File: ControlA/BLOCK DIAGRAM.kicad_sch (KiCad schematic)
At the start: 0 parts

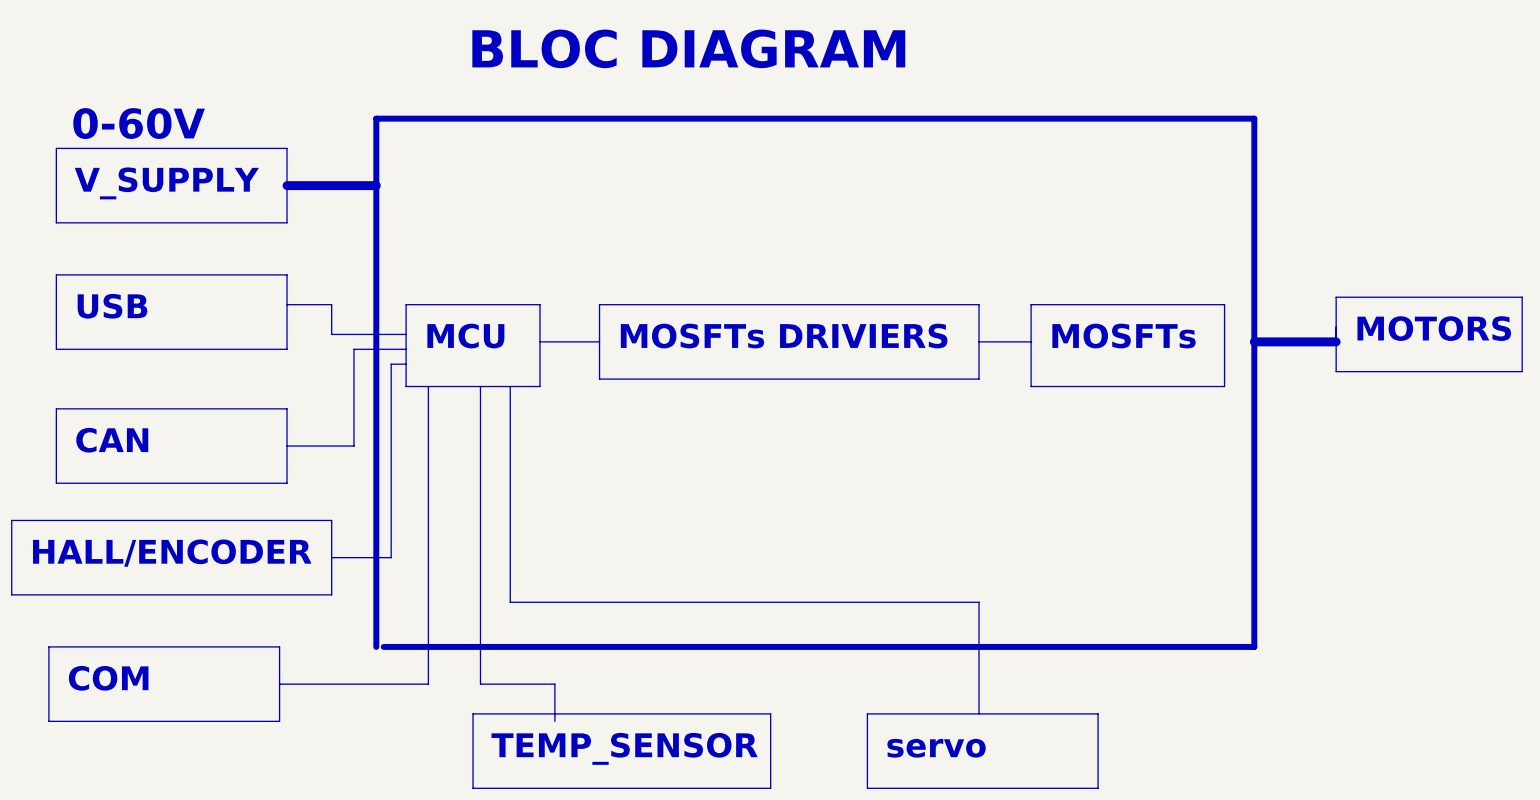
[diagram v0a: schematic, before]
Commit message: add libray symbole and add sheet
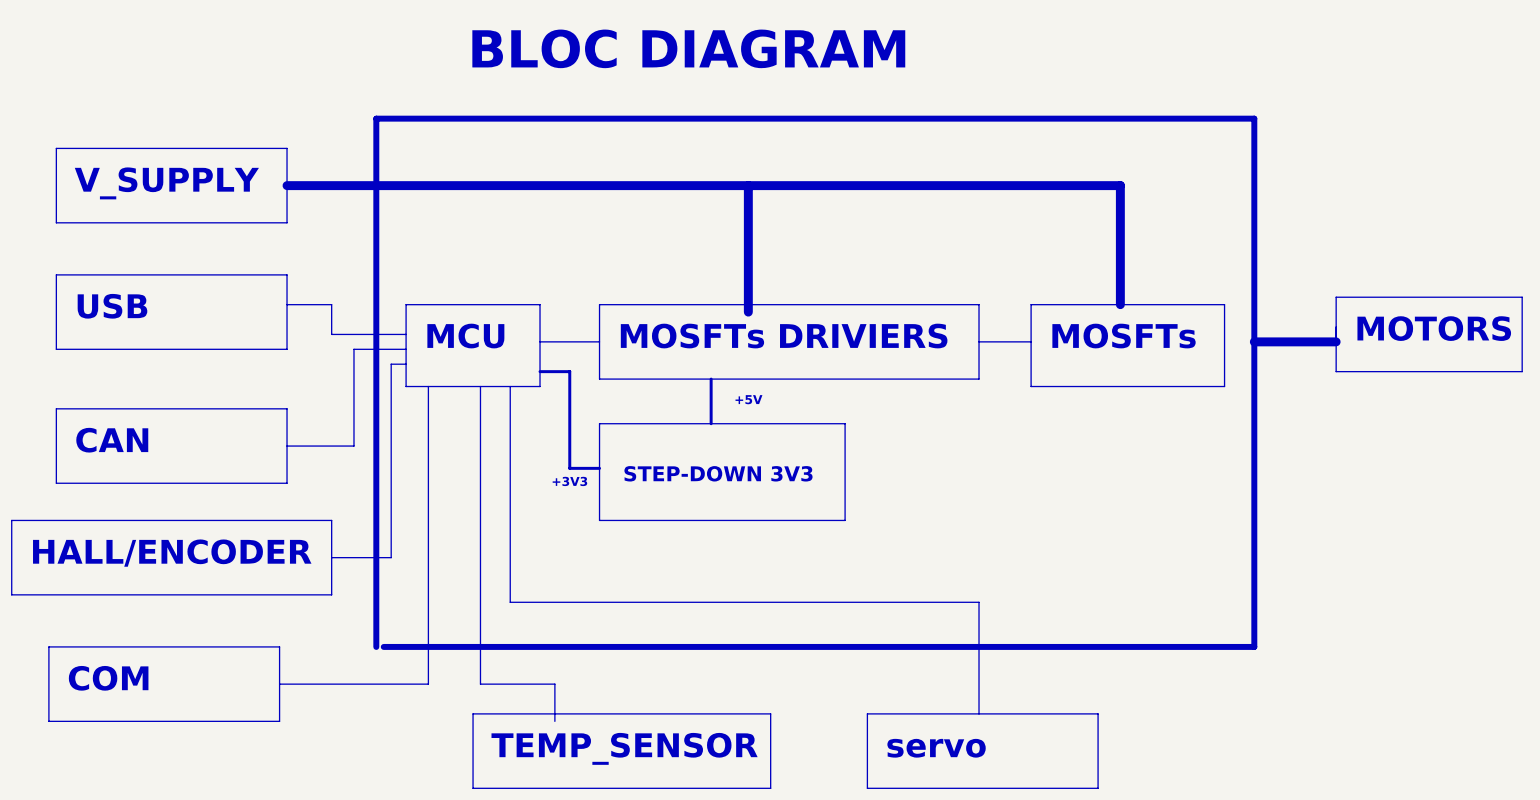
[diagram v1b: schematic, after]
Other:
- note added: "+3V3"
- note added: "+5V"
- note added: "STEP-DOWN 3V3"
- note removed: "0-60V"
- company: (none) -> DR SYSTEMS
- title: (none) -> BLOCK DIGRAM ESC
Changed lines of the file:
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@@
 	(generator_version "8.0")
 	(paper "A4")
+	(title_block
+		(title "BLOCK DIGRAM ESC")
+		(date "2024-06-21")
+		(rev "RACHID RAHEL")
+		(company "DR SYSTEMS")
+		(comment 1 "modification")
+	)
 	(polyline
 		(pts
@@
 			(width 1.016)
 			(type default)
+			(color 0 132 0 1)
 		)
 	)
@@
 	(polyline
 		(pts
+			(xy 142.24 80.01) (xy 142.24 87.63)
+		)
+		(stroke
+			(width 0.508)
+			(type default)
+			(color 255 0 0 1)
+		)
+	)
+	(polyline
+		(pts
 			(xy 102.87 81.28) (xy 102.87 132.08)
 		)
@@
 			(width 0)
 			(type default)
+		)
+	)
+	(polyline
+		(pts
+			(xy 148.59 46.99) (xy 148.59 68.58)
+		)
+		(stroke
+			(width 1.524)
+			(type default)
+			(color 255 0 0 1)
 		)
 	)
@@
 			(width 1.016)
 			(type solid)
+			(color 0 132 0 1)
+		)
+	)
+	(polyline
+		(pts
+			(xy 113.03 78.74) (xy 118.11 78.74)
+		)
+		(stroke
+			(width 0.508)
+			(type default)
+			(color 255 0 0 1)
+		)
+	)
+	(polyline
+		(pts
+			(xy 212.09 46.99) (xy 212.09 67.31)
+		)
+		(stroke
+			(width 1.524)
+			(type default)
+			(color 255 0 0 1)
 		)
 	)
@@
 	(polyline
 		(pts
+			(xy 118.11 78.74) (xy 118.11 95.25)
+		)
+		(stroke
+			(width 0.508)
+			(type default)
+			(color 255 0 0 1)
+		)
+	)
+	(polyline
+		(pts
 			(xy 68.58 132.08) (xy 93.98 132.08)
 		)
@@
 	(polyline
 		(pts
+			(xy 120.65 95.25) (xy 123.19 95.25)
+		)
+		(stroke
+			(width 0)
+			(type default)
+		)
+	)
+	(polyline
+		(pts
 			(xy 187.96 118.11) (xy 187.96 137.16)
 		)
@@
 	(polyline
 		(pts
+			(xy 118.11 95.25) (xy 123.19 95.25)
+		)
+		(stroke
+			(width 0.508)
+			(type default)
+			(color 255 0 0 1)
+		)
+	)
+	(polyline
+		(pts
+			(xy 142.24 80.01) (xy 142.24 87.63)
+		)
+		(stroke
+			(width 0)
+			(type default)
+		)
+	)
+	(polyline
+		(pts
 			(xy 234.95 125.73) (xy 234.95 35.56)
 		)
@@
 			(width 1.016)
 			(type default)
+			(color 0 132 0 1)
 		)
 	)
@@
 			(width 1.016)
 			(type default)
+			(color 0 132 0 1)
+		)
+	)
+	(polyline
+		(pts
+			(xy 120.65 95.25) (xy 123.19 95.25)
+		)
+		(stroke
+			(width 0)
+			(type default)
 		)
 	)
@@
 	(polyline
 		(pts
-			(xy 85.09 46.99) (xy 85.09 45.72)
-		)
-		(stroke
-			(width 0)
-			(type default)
-		)
-	)
-	(polyline
-		(pts
-			(xy 69.85 46.99) (xy 85.09 46.99)
+			(xy 69.85 46.99) (xy 212.09 46.99)
 		)
 		(stroke
 			(width 1.524)
 			(type default)
+			(color 255 0 0 1)
 		)
 	)
@@
 			(width 0)
 			(type default)
+		)
+	)
+	(rectangle
+		(start 123.19 87.63)
+		(end 165.1 104.14)
+		(stroke
+			(width 0)
+			(type default)
+		)
+		(fill
+			(type none)
 		)
 	)
@@
 		)
 	)
+	(text "+3V3"
+		(exclude_from_sim no)
+		(at 118.11 97.79 0)
+		(effects
+			(font
+				(size 1.524 1.524)
+				(bold yes)
+				(color 255 0 0 1)
+			)
+		)
+	)
 	(text "BLOC DIAGRAM"
 		(exclude_from_sim no)
@@
 		)
 	)
-	(text "0-60V"
-		(exclude_from_sim no)
-		(at 44.45 36.83 0)
-		(effects
-			(font
-				(size 5.08 5.08)
-				(bold yes)
-			)
-		)
+	(text "STEP-DOWN 3V3"
+		(exclude_from_sim no)
+		(at 143.51 96.52 0)
+		(effects
+			(font
+				(size 2.54 2.54)
+				(bold yes)
+			)
+		)
+	)
+	(text "+5V"
+		(exclude_from_sim no)
+		(at 148.59 83.82 0)
+		(effects
+			(font
+				(size 1.524 1.524)
+				(bold yes)
+				(color 255 0 0 1)
+			)
+		)
